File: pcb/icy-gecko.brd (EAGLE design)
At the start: 160 x 100 mm, 4 parts, among them J1 USB-C, U1 EFM32GG12B8XX_QFN64, U2 ICE40LP384-SG32, U3 MIC23159

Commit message: sch work
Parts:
- added D1: SK9822, Opto-electronics > LED Emitters:2020
- added D2: B0530W, Semiconductors > Discrete Semiconductors > Diodes & Rectifiers > Schottky Diodes & Rectifiers:SOD-123
- added F1: (no value), Circuit Protection > Resettable Fuses - PPTC:PTC1210
- added SW1: (no value), Eletromechanical > Switches > Tactile Switches:PUSH_BUTTON
- added U4: W25Q40BVZP, Semiconductors > Integrated Circuits - ICs > Memory ICs > Flash:WSON8
- moved U2 1.43 mm to (-7.50, -14.1)
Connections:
- new net GND: U4.4
- new net VCC: U4.8
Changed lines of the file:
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@@
 <attribute name="NAME" x="-8.276" y="-9.5" size="0.8" layer="25" font="vector" ratio="12" align="center"/>
 </element>
-<element name="U2" library="Semiconductors &gt; Embedded Processors &amp; Controllers &gt; FPGA - Field Programmable Gate Array" package="QFN32" value="ICE40LP384-SG32" x="-6.1" y="-14.4" smashed="yes">
-<attribute name="NAME" x="-8.64" y="-10.971" size="0.8" layer="25" font="vector" ratio="12" align="center"/>
+<element name="U2" library="Semiconductors &gt; Embedded Processors &amp; Controllers &gt; FPGA - Field Programmable Gate Array" package="QFN32" value="ICE40LP384-SG32" x="-7.5" y="-14.1" smashed="yes">
+<attribute name="NAME" x="-10.04" y="-10.671" size="0.8" layer="25" font="vector" ratio="12" align="center"/>
 </element>
 <element name="U3" library="Power &gt; Switching Controllers" package="VQFN20" value="MIC23159" x="-15" y="-14.8" smashed="yes">
 <attribute name="NAME" x="-17.54" y="-10.99" size="1.27" layer="25"/>
 </element>
+<element name="U4" library="Semiconductors &gt; Integrated Circuits - ICs &gt; Memory ICs &gt; Flash" package="WSON8" value="W25Q40BVZP" x="-14.9" y="5.8" smashed="yes">
+<attribute name="NAME" x="-18.6925" y="2.99" size="1.016" layer="25" ratio="18" rot="R90"/>
+</element>
+<element name="F1" library="Circuit Protection &gt; Resettable Fuses - PPTC" package="PTC1210" value="" x="-25" y="-12.8" smashed="yes">
+<attribute name="NAME" x="-27.54" y="-10.26" size="1.27" layer="25"/>
+<attribute name="VALUE" x="-27.54" y="-16.61" size="1.27" layer="27"/>
+</element>
+<element name="D1" library="Opto-electronics &gt; LED Emitters" package="2020" value="SK9822" x="-25.9" y="-18.7" smashed="yes">
+<attribute name="NAME" x="-25.9" y="-20.3" size="0.8" layer="21" font="vector" ratio="12" align="center"/>
+</element>
+<element name="SW1" library="Eletromechanical &gt; Switches &gt; Tactile Switches" package="PUSH_BUTTON" value="" x="-23.6" y="-23.7" smashed="yes">
+<attribute name="NAME" x="-24.489" y="-21.922" size="0.4064" layer="25"/>
+<attribute name="VALUE" x="-24.489" y="-25.732" size="0.4064" layer="27"/>
+</element>
+<element name="D2" library="Semiconductors &gt; Discrete Semiconductors &gt; Diodes &amp; Rectifiers &gt; Schottky Diodes &amp; Rectifiers" package="SOD-123" value="B0530W" x="-25.4" y="-28" smashed="yes">
+<attribute name="NAME" x="-26.5" y="-27" size="0.4064" layer="25"/>
+<attribute name="VALUE" x="-26.5" y="-29.284" size="0.4064" layer="27"/>
+</element>
 </elements>
 <signals>
+<signal name="GND">
+<contactref element="U4" pad="4"/>
+</signal>
+<signal name="VCC">
+<contactref element="U4" pad="8"/>
+</signal>
 </signals>
 <mfgpreviewcolors>

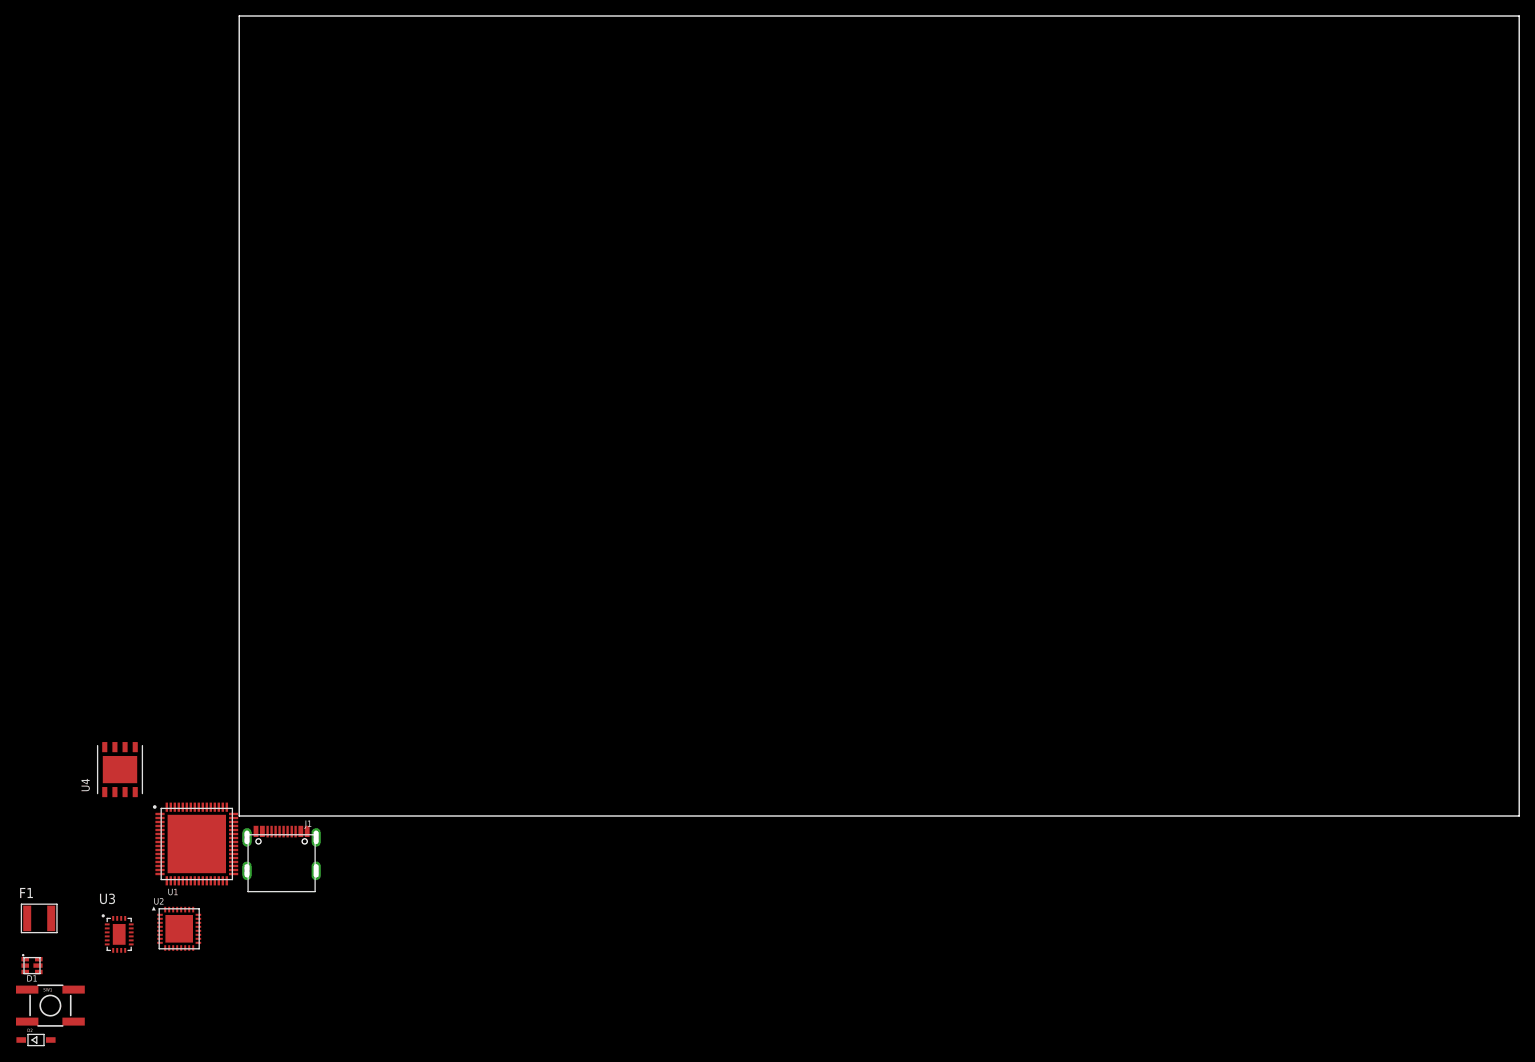
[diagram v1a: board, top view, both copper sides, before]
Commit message: finish sch, scrap pcb
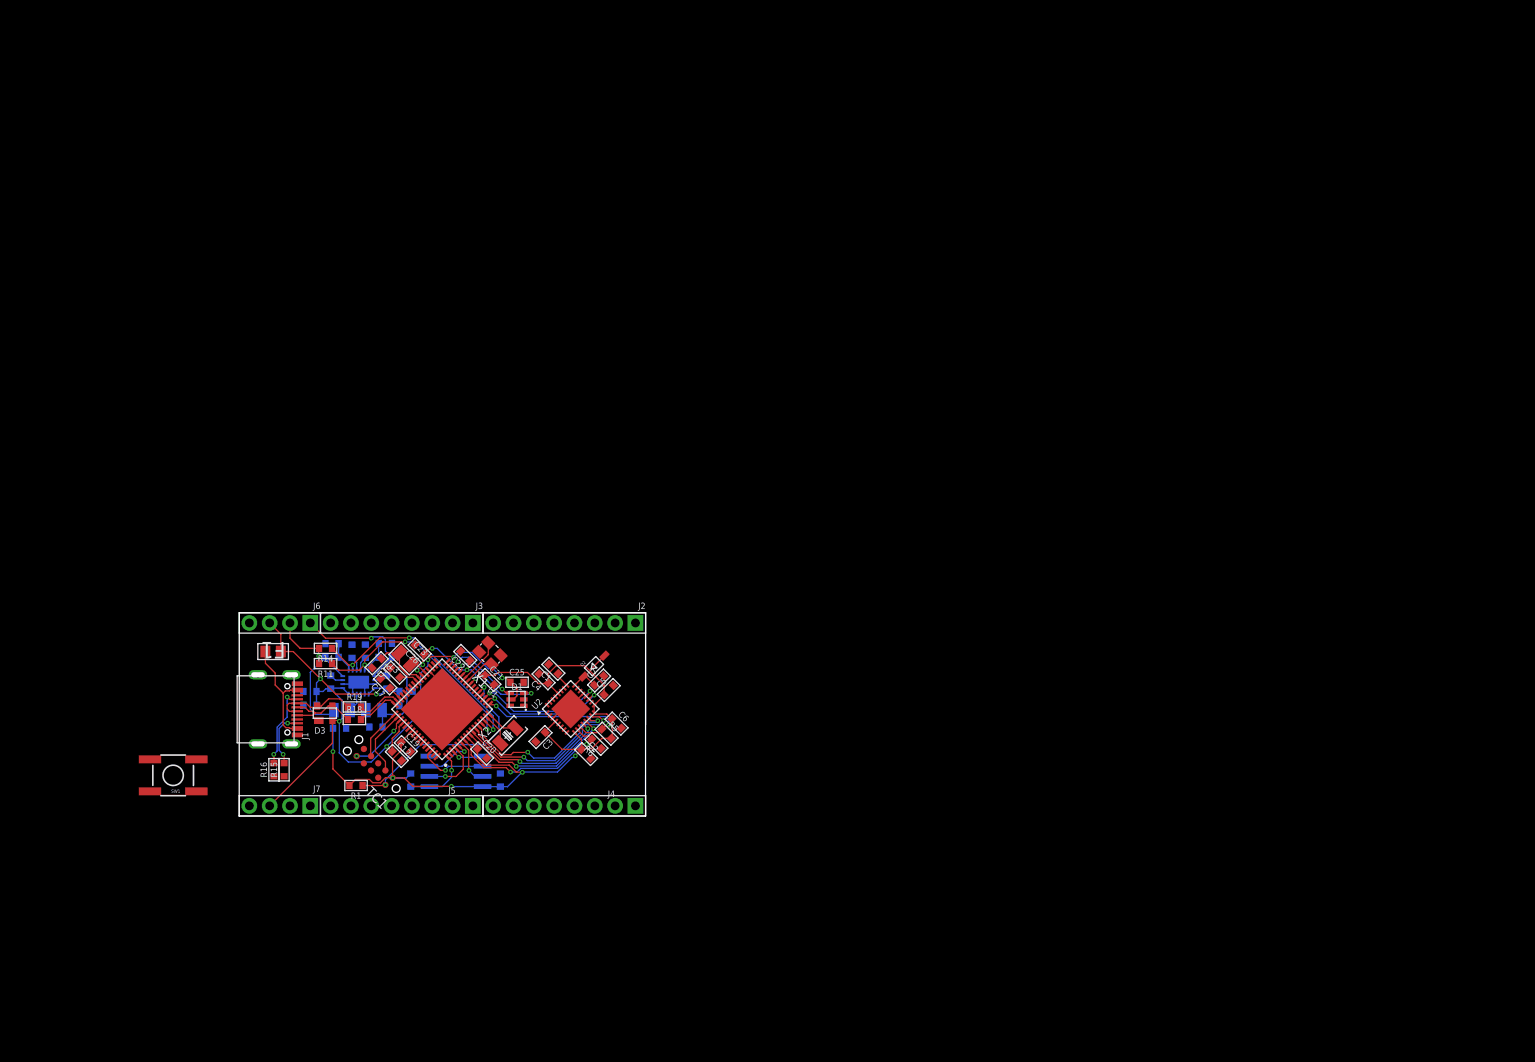
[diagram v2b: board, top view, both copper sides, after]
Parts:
- removed U4: W25Q40BVZP, Semiconductors > Integrated Circuits - ICs > Memory ICs > Flash:WSON8
- added C1, C19, C2, C20, C21, C22, C24, C25, C3, C4, C5, C6, C7: 100n, Passive Components > Capacitors > Multilayer Ceramic Capacitors MLCC:0603_WAVE
- added C10, C13: 470p, Passive Components > Capacitors > Multilayer Ceramic Capacitors MLCC:0603_WAVE
- added C11, C14, C15, C8: 10u, Passive Components > Capacitors > Multilayer Ceramic Capacitors MLCC:0603_WAVE
- added C12, C17, C18, C23, C26: 4u7, Passive Components > Capacitors > Multilayer Ceramic Capacitors MLCC:0603_WAVE
- added C16, C9: 1u, Passive Components > Capacitors > Multilayer Ceramic Capacitors MLCC:0603_WAVE
- added D3: SP0503BAHT, Circuit Protection > ESD Suppressors \ TVS Diodes:SOT143
- added J2, J3, J4, J5: 8, Connectors > Header:1X8_2.54
- added J6, J7: 4, Connectors > Header:1X4_2.54
- added L1, L2, L3: 1u, Passive Components > Inductors, Chokes & Coils:_0806
- added R1, R6: 10k, Passive Components > Resistors > Chip Resistors:0603_WAVE
- added R10, R11, R14, R17, R7: 100k, Passive Components > Resistors > Chip Resistors:0603_WAVE
- added R12: 274k, Passive Components > Resistors > Chip Resistors:0603_WAVE
- added R13: 294k, Passive Components > Resistors > Chip Resistors:0603_WAVE
- added R15, R16: 5k11, Passive Components > Resistors > Chip Resistors:0603_WAVE
- added R18, R19: 22, Passive Components > Resistors > Chip Resistors:0603_WAVE
- added R5: 2k2, Passive Components > Resistors > Chip Resistors:0603_WAVE
- added R8: 309k, Passive Components > Resistors > Chip Resistors:0603_WAVE
- added R9: 71k5, Passive Components > Resistors > Chip Resistors:0603_WAVE
- added TC1: TC2050-IDC-NL, Connectors > Other:TC2050-IDC-NL
- added U6: SST26VF016B, Microchip:WSOIC8
- added X1: (no value), Passive Components > Frequency Control & Timing Devices > Crystals:4-SMD-3225
- added X2: (no value), Passive Components > Frequency Control & Timing Devices > Crystals:2-SMD-3215
- F1: value (none) -> 100mA; device Circuit Protection > Resettable Fuses - PPTC:PTC1210 -> Circuit Protection > Resettable Fuses - PPTC:0805
- moved D2 84.0 mm to (44.4, 18.7), turned to 45 degrees
- moved D1 69.2 mm to (34.7, 14.6), turned to 180 degrees
- moved U2 56.1 mm to (41.4, 13.4), turned to 45 degrees
- moved F1 44.4 mm to (4.24, 20.6), turned to 180 degrees
- moved U3 43.5 mm to (14.9, 16.7), flipped to the bottom, turned to 90 degrees
- moved U1 35.0 mm to (25.4, 13.3), turned to 135 degrees
- moved SW1 32.6 mm to (-8.26, 5.08), turned to 180 degrees
- moved J1 23.1 mm to (0.00, 13.3), turned to 270 degrees
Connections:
- removed net VCC: U4.8
- new net !CRESET: R6.P$2, U1.7, U2.10
- new net !MCU_RESET: R1.P$1, SW1.1, TC1.10, U1.21
- new net 1.2V: C1.P$1, C14.P$1, J6.1, J7.1, L2.1, R12.P$1, U2.25, U3.17
- new net 1V2_PG: R11.P$1, U1.13, U3.15
- new net 3.3V: C11.P$1, C19.P$1, C2.P$1, C20.P$1, C21.P$1, C22.P$1, C24.P$1, C26.P$1, C3.P$1, C4.P$1, C5.P$1, C6.P$1, D2.A, J6.2, J7.2, L1.1, R1.P$2, R11.P$2, R14.P$2, R17.P$2, R5.P$2, R8.P$2, TC1.1, U1.24, U1.27, U1.38, U1.55, U1.8, U2.16, U2.17, U2.28, U2.4, U2.9, U3.10, U6.8
- new net 3V3_PG: R14.P$1, U1.14, U3.12
- new net CDONE: R5.P$1, U1.17, U2.11
- new net CLK: U1.18, U2.19
- new net DN: R19.P$2, U1.47
- new net DP: R18.P$2, U1.48
- new net GPRST: U1.19, U2.20
- new net IOL_2A: U2.2
- new net IOL_2B: U2.1
- new net IOL_4A: U2.5
- new net IOL_4B_GBIN7: U2.6
- new net IOL_5A_GBIN6: U2.8
- new net IOL_5B: U2.7
- new net IOR_34: U2.18
- new net IOR_38: U2.22
- new net IOR_39: U2.23
- new net IOT_45: U2.26
- new net IOT_47: U2.27
- new net IOT_49_GBIN0: U2.29
- new net IOT_50_GBIN1: U2.30
- new net IOT_52: U2.32
- new net IOT_53: U2.31
- new net LED_CLK: D1.4, U1.30
- new net LED_MOSI: D1.3, U1.28
- new net MAIN_HFXTAL_N: U1.25, X1.1
- new net MAIN_HFXTAL_P: U1.26, X1.3
- new net MAIN_LFXTAL_N: U1.16, X2.2
- new net MAIN_LFXTAL_P: U1.15, X2.1
- new net MISO: U1.10, U2.12
- new net MOSI: U1.9, U2.13
- new net MPU_PWR: R10.P$1, U3.18
- new net N$1: C7.P$1, D2.C, U2.24
- new net N$32: R7.P$1, U3.9
- new net N$33: L1.2, U3.4
- new net N$34: C10.P$1, U3.13
- new net N$35: R8.P$1, R9.P$2, U3.11
- new net N$36: L2.2, U3.3
- new net N$37: C13.P$1, U3.14
- new net N$38: R12.P$2, R13.P$1, U3.16
- new net N$39: C17.P$1, U1.46
- new net N$40: F1.2, J1.A4/B9, J1.B4/A9
- new net N$41: J1.B5, R15.P$2
- new net N$42: J1.A5, R16.P$2
- new net N$43: L3.1, U1.37
- new net N$45: C23.P$1, U1.40
- new net N$48: C18.P$1, L3.2, U1.39
- new net PD3: U1.31
- new net PD4: U1.32
- new net PD5: U1.33
- new net PD6: U1.34
- new net PE10: U1.58
- new net PE11: U1.59
- new net PE12: U1.60
- new net PE13: U1.61
- new net PE4: U1.41
- new net PE5: U1.42
- new net PE6: U1.43
- new net PE7: U1.44
- new net PE8: U1.56
- new net PE9: U1.57
- new net PF12: U1.53
- new net QSPI_CLK: U1.62, U6.6
- new net QSPI_CS0: R17.P$1, U1.1, U6.1
- new net QSPI_D0: U1.3, U6.5
- new net QSPI_D1: U1.4, U6.2
- new net QSPI_D2: U1.5, U6.3
- new net QSPI_D3: U1.6, U6.7
- new net SCK: U1.11, U2.15
- new net SS: U1.12, U2.14
- new net SWCLK: TC1.4, U1.49
- new net SWDIO: TC1.2, U1.50
- new net SWO: TC1.6, U1.51
- new net USBDN: D3.4, J1.A7, J1.B7, R19.P$1
- new net USBDP: D3.3, J1.A6, J1.B6, R18.P$1
- new net VUSB: C12.P$1, C15.P$1, C16.P$1, C25.P$1, C8.P$1, C9.P$1, D1.5, D3.2, F1.1, J6.3, J7.3, R10.P$2, R7.P$2, U1.52, U3.1, U3.20, U3.6, U3.7
- net GND: now also C1.P$2, C10.P$2, C11.P$2, C12.P$2, C13.P$2, C14.P$2, C15.P$2, C16.P$2, C17.P$2, C18.P$2, C19.P$2, C2.P$2, C20.P$2, C21.P$2, C22.P$2, C23.P$2, C24.P$2, C25.P$2, C26.P$2, C3.P$2, C4.P$2, C5.P$2, C6.P$2, C7.P$2, C8.P$2, C9.P$2, D1.2, D3.1, J1.A1/B12, J1.B1/A12, J1.SHIELD0, J1.SHIELD1, J1.SHIELD2, J1.SHIELD3, J3.1, J4.8, J6.4, J7.4, R13.P$2, R15.P$1, R16.P$1, R6.P$1, R9.P$1, SW1.3, SW1.4, TC1.3, TC1.9, U1.36, U1.65, U2.21, U2.3, U2.33, U3.19, U3.2, U3.21, U3.5, U3.8, U6.4, X1.2, X1.4; no longer U4.4
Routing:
- net 3.3V: track 0.00 -> 147.0 mm, vias 0 -> 11
- net VUSB: track 0.00 -> 98.3 mm, vias 0 -> 7
- net 1.2V: track 0.00 -> 31.1 mm, vias 0 -> 1
- net 3V3_PG: track 0.00 -> 30.5 mm, vias 0 -> 3
- net 1V2_PG: track 0.00 -> 29.0 mm, vias 0 -> 3
- net !MCU_RESET: track 0.00 -> 27.5 mm, vias 0 -> 2
- net SCK: track 0.00 -> 22.3 mm, vias 0 -> 2
- net !CRESET: track 0.00 -> 22.3 mm, vias 0 -> 2
- net SS: track 0.00 -> 21.0 mm, vias 0 -> 2
- net CDONE: track 0.00 -> 20.7 mm, vias 0 -> 2
- net MOSI: track 0.00 -> 20.6 mm, vias 0 -> 2
- net MISO: track 0.00 -> 19.0 mm, vias 0 -> 2
- net GND: track 0.00 -> 18.9 mm
- net GPRST: track 0.00 -> 16.5 mm, vias 0 -> 2
- net CLK: track 0.00 -> 16.4 mm, vias 0 -> 2
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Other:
- board size 160 x 100 mm -> 50.8 x 25.4 mm

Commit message: pcd finito
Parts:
- moved R17 25.2 mm to (46.5, 6.37), flipped to the top, turned to 270 degrees
- moved SW1 23.9 mm to (15.2, 9.53)
- moved R11 20.7 mm to (26.4, 32.7), turned to 270 degrees
- moved J2 19.8 mm to (61.0, 38.1)
- moved J3 19.8 mm to (40.6, 38.1)
- moved J6 19.8 mm to (20.3, 38.1)
- moved C8 19.5 mm to (24.2, 27.6), flipped to the top
- moved C9 19.5 mm to (24.2, 25.9), flipped to the top
- moved R14 18.0 mm to (24.5, 32.7), turned to 270 degrees
- moved C25 16.2 mm to (37.9, 32.6)
- moved D1 16.2 mm to (37.9, 30.4)
- moved C1 15.8 mm to (54.0, 24.1)
- moved R7 15.8 mm to (21.6, 28.8), flipped to the top
- moved D2 15.8 mm to (59.0, 24.5)
- moved C2 15.7 mm to (58.0, 13.5)
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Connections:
- net 1V2_PG: now also U1.29; no longer U1.13
- net 3V3_PG: now also U1.35; no longer U1.14
- net IOL_2A: now also J4.5
- net IOL_2B: now also J4.6
- net IOL_4A: now also J4.4
- net IOL_4B_GBIN7: now also J4.3
- net IOL_5A_GBIN6: now also J4.1
- net IOL_5B: now also J4.2
- net IOR_34: now also J2.1
- net IOR_38: now also J2.2
- net IOR_39: now also J2.3
- net IOT_45: now also J2.4
- net IOT_47: now also J2.5
- net IOT_49_GBIN0: now also J2.6
- net IOT_50_GBIN1: now also J2.7
- net IOT_52: now also J4.7
- net IOT_53: now also J2.8
- net PD3: now also J3.2
- net PD4: now also J3.3
- net PD5: now also J3.4
- net PD6: now also J3.5
- net PE10: now also J5.4
- net PE11: now also J5.3
- net PE12: now also J5.2
- net PE13: now also J5.1
- net PE4: now also J3.6
- net PE5: now also J3.7
- net PE6: now also J5.8
- net PE7: now also J5.7
- net PE8: now also J5.6
- net PE9: now also J5.5
- net PF12: now also J3.8
- net USBDP: now also D3.2; no longer D3.3
- net VUSB: now also D3.3; no longer D3.2
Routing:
- net 1.2V: track 31.1 -> 103.5 mm, vias 1 -> 3
- net 3.3V: track 147.0 -> 203.1 mm, vias 11 -> 9
- net PE6: track 0.00 -> 29.5 mm, vias 0 -> 3
- net PE7: track 0.00 -> 27.4 mm, vias 0 -> 3
- net PF12: track 0.00 -> 27.0 mm, vias 0 -> 2
- net IOT_53: track 0.00 -> 23.0 mm, vias 0 -> 1
- net IOT_50_GBIN1: track 0.00 -> 21.5 mm, vias 0 -> 1
- net IOT_47: track 0.00 -> 21.3 mm, vias 0 -> 1
- net IOT_49_GBIN0: track 0.00 -> 21.0 mm, vias 0 -> 1
- net IOR_34: track 0.00 -> 20.5 mm, vias 0 -> 1
- net PE4: track 0.00 -> 20.3 mm
- net PE5: track 0.00 -> 20.1 mm
- net IOT_45: track 0.00 -> 19.9 mm, vias 0 -> 1
- net IOT_52: track 0.00 -> 19.7 mm, vias 0 -> 1
- net IOL_2A: track 0.00 -> 18.9 mm, vias 0 -> 1
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- added copper zone on layer 1, net GND
- added copper zone on layer 16, net GND
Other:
- board size 50.8 x 25.4 mm -> 65.4 x 40 mm

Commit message: sync
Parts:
- added U$1: (no value), Utility > Silkscreen:GECKO_POLY
- added U$2: (no value), Utility > Silkscreen:OSHW-LOGO-M
- added U$3: (no value), Utility > Silkscreen:RAFAEL_SILVA_5MM_ALT_3
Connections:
- net IOL_4A renamed IOL4A
- net IOL_4B_GBIN7 renamed IOL4BG7
- net IOL_5A_GBIN6 renamed IOL5AG6
- net IOL_5B renamed IOL5B
- net IOR_34 renamed IOR34
- net IOR_38 renamed IOR38
- net IOR_39 renamed IOR39
- net IOT_45 renamed IOT45
- net IOT_47 renamed IOT47
- net IOT_49_GBIN0 renamed IOT49G0
- net IOT_50_GBIN1 renamed IOT50G1
- net IOT_52 renamed IOT52
- net IOT_53 renamed IOT53
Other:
- board text added: "1V2"
- board text added: "3V3"
- board text added: "Designed in Portugal"
- board text added: "GND"
- board text added: "IOL2A"
- board text added: "IOL2B"
- board text added: "IOL4A"
- board text added: "IOL4BG7"
- board text added: "IOL5AG6"
- board text added: "IOL5B"
- board text added: "IOR34"
- board text added: "IOR38"
- board text added: "IOR39"
- board text added: "IOT45"
- board text added: "IOT47"
- board text added: "IOT49G0"
- board text added: "IOT50G1"
- board text added: "IOT52"
- board text added: "IOT53"
- board text added: "Icy-Gecko HV1.0 #2519"
- board text added: "MCU: EFM32GG12B810 FPGA: ICE40LP384"
- board text added: "PD4"
- board text added: "PD5"
- board text added: "PD6"
- board text added: "PE10"
- board text added: "PE11"
- board text added: "PE12"
- board text added: "PE13"
- board text added: "PE4"
- board text added: "PE5"
- board text added: "PE6"
- board text added: "PE7"
- board text added: "PE8"
- board text added: "PE9"
- board text added: "PF12"
- board text added: "VUSB"

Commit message: corrected some pcb errors
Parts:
- removed J1: USB-C, Connectors > USB:USB-C
- added USB1: USB-C-16P-SMD-FLAT-SIDE-TYPE-2, Connectors > USB:USB-C-16P-SMD-FLAT-SIDE-TYPE-2
- L3: value 1u -> 4u7
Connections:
- net GND: now also USB1.A1/B12, USB1.B1/A12, USB1.SHIELD@0, USB1.SHIELD@1, USB1.SHIELD@2, USB1.SHIELD@3; no longer J1.A1/B12, J1.B1/A12, J1.SHIELD0, J1.SHIELD1, J1.SHIELD2, J1.SHIELD3
- net N$40: now also USB1.A4/B9, USB1.B4/A9; no longer J1.A4/B9, J1.B4/A9
- net N$41: now also USB1.B8; no longer J1.B5
- net N$42: now also USB1.A8; no longer J1.A5
- net USBDN: now also USB1.A7, USB1.B7; no longer J1.A7, J1.B7
- net USBDP: now also USB1.A6, USB1.B6; no longer J1.A6, J1.B6
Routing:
- net N$41: track 8.68 -> 11.9 mm
- net 3.3V: track 203.1 -> 204.9 mm
